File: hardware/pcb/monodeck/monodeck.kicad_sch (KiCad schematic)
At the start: 12 parts

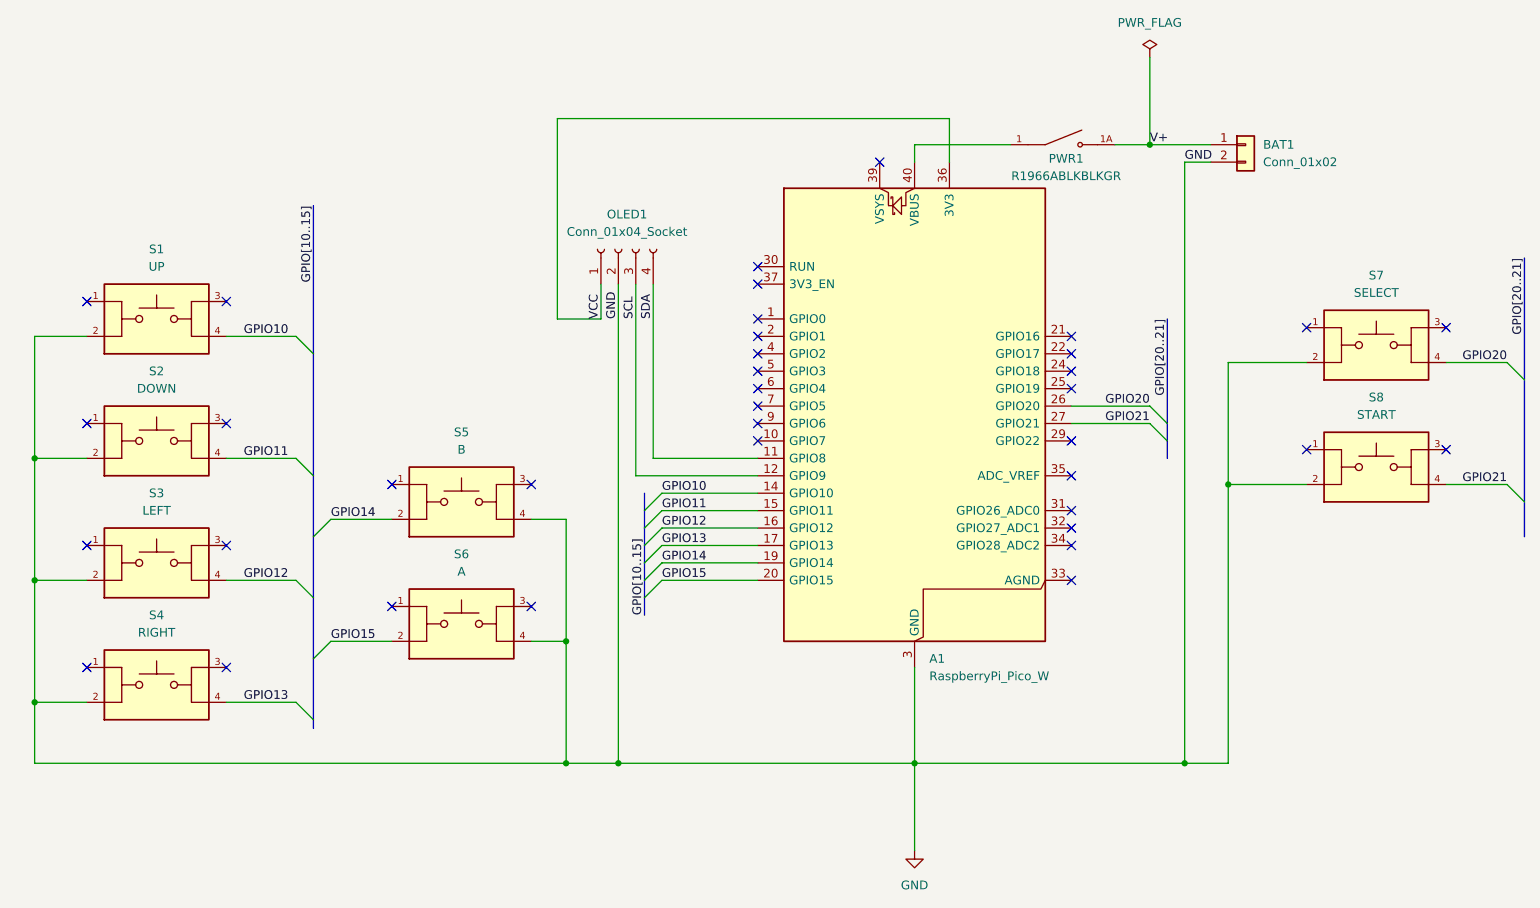
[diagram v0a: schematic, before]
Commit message: updated schematic and pcb, replaced pico smd with pin sockets
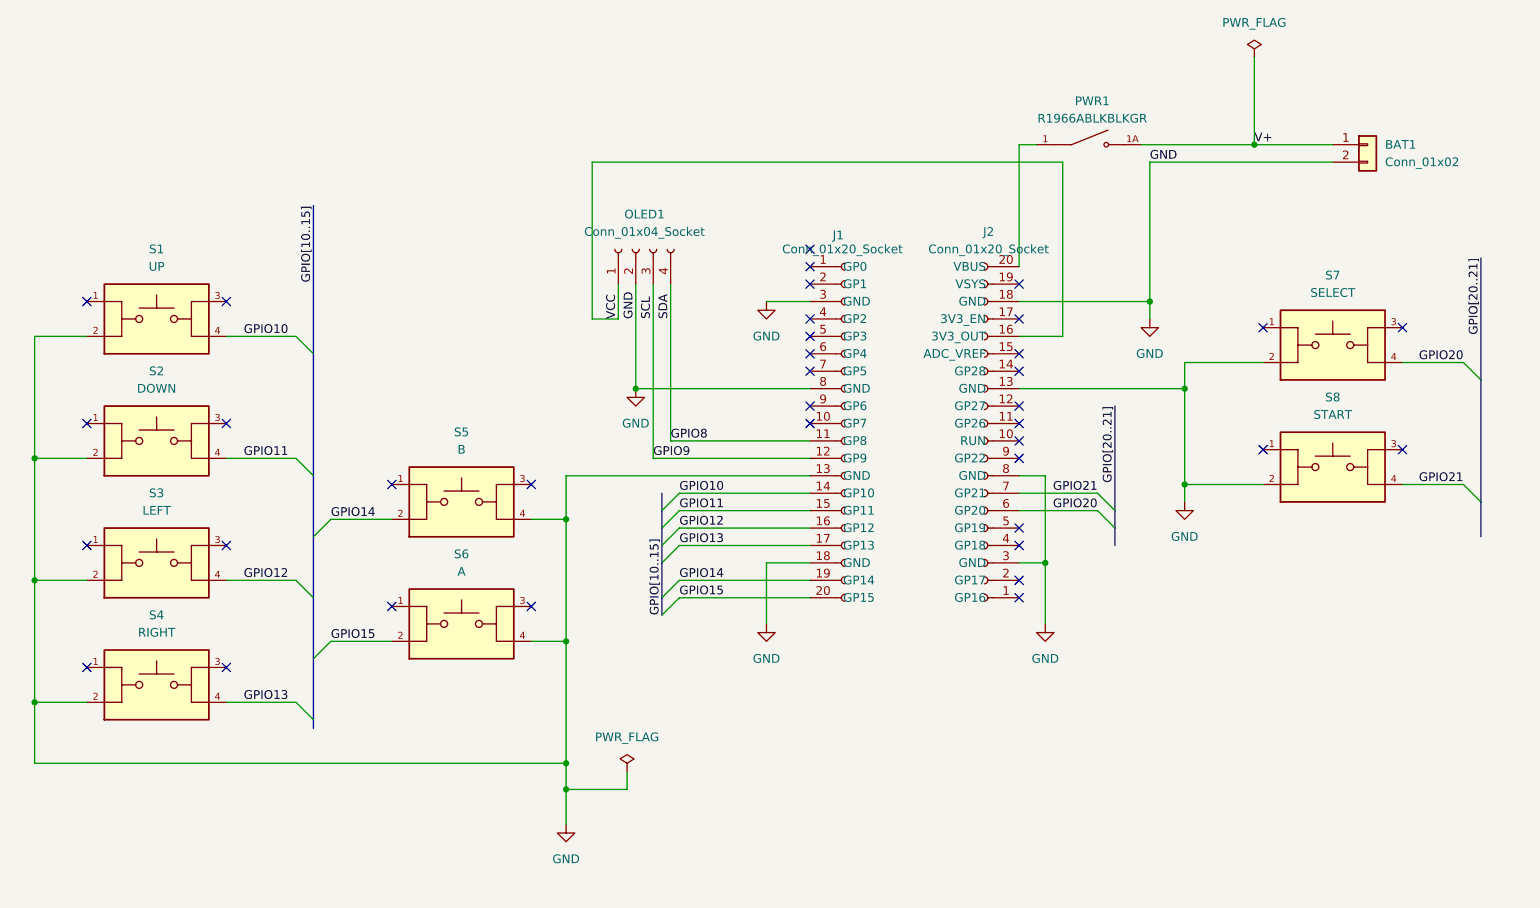
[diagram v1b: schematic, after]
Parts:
- removed A1: RaspberryPi_Pico_W, Module:RaspberryPi_Pico_W_SMD_HandSolder, symbol MCU_Module:RaspberryPi_Pico_W
- added J1, J2: Conn_01x20_Socket, Connector_PinSocket_2.54mm:PinSocket_1x20_P2.54mm_Vertical, symbol Connector:Conn_01x20_Socket
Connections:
- net GND: now also J1.13 (GND), J1.18 (GND), J1.3 (GND), J1.8 (GND), J2.13 (GND), J2.18 (GND), J2.3 (GND), J2.8 (GND)
- net GPIO10: now also J1.14 (GP10)
- net GPIO11: now also J1.15 (GP11)
- net GPIO12: now also J1.16 (GP12)
- net GPIO13: now also J1.17 (GP13)
- net GPIO14: now also J1.19 (GP14)
- net GPIO15: now also J1.20 (GP15)
- net GPIO20: now also J2.6 (GP20)
- net GPIO21: now also J2.7 (GP21)
- net VCC: now also J2.16 (3V3_OUT)
- net at PWR1.1: now also J2.20 (VBUS)
- net SCL renamed GPIO9
- net GPIO9: now also J1.12 (GP9)
- net SDA renamed GPIO8
- net GPIO8: now also J1.11 (GP8)
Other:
- moved on the sheet: BAT1, OLED1, PWR1, S7, S8

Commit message: added tp4056 module to the circuit
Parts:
- added U1: TP4056, TP4056-Module:TP4056-Module, symbol TP4056-Module:Tp4056-Module
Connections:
- net GND: now also U1.4 (Vout-), U1.6 (B-)
- net V+: now also J2.20 (VBUS); no longer BAT1.1 (Pin_1)
- net at PWR1.1: now also U1.3 (Vout+); no longer J2.20 (VBUS)
- new net: BAT1.1 (Pin_1), U1.5 (B+)
- no-connect marks 37 -> 38
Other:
- moved on the sheet: BAT1, PWR1

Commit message: finished first iteration of pcb
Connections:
- net GND: no longer J1.13 (GND), J1.3 (GND), J1.8 (GND), J2.13 (GND), J2.18 (GND), S1.2, S2.2, S3.2, S4.2, S5.4, S6.4, S7.2, S8.2
- net GPIO11: now also S2.3; no longer S2.4
- net GPIO13: now also S4.3; no longer S4.4
- net GPIO20: now also S5.1; no longer S7.4
- net GPIO21: now also S6.1; no longer S8.4
- net GND1: now reaches S1.1
- net GND1: now also J1.3 (GND), S2.1, S2.2, S3.1, S4.2
- net GPIO2: now reaches J1.4 (GP2)
- net GPIO2: now also S8.3
- net GPIO3: now reaches J1.5 (GP3)
- net GPIO3: now also S7.3
- net GPIO14: no longer names the net of J1.19 (GP14)
- net GPIO14: no longer S5.2
- net GPIO15: no longer names the net of J1.20 (GP15)
- net GPIO15: no longer S6.2
- new net GND2: J2.18 (GND), S5.4, S6.4, S7.2, S8.2
- no-connect marks 38 -> 40
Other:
- moved on the sheet: S5, S6

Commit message: update: edited gnd plane to connect all gnd nets
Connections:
- net GND1 is gone; now on net GND: J1.3 (GND), S1.1, S2.1, S2.2, S3.1, S4.2
- net GND2 is gone; now on net GND: J2.18 (GND), S5.4, S6.4, S7.2, S8.2

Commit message: updated pcb and dpad pin mapping for efficient routing
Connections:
- net GPIO10: now also S4.3; no longer S1.4
- net GPIO11: now also S1.4; no longer S2.3
- net GPIO12: now also S2.3; no longer S3.4
- net GPIO13: now also S3.4; no longer S4.3
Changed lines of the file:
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@@
 		)
 	)
-	(label "GPIO11"
+	(label "GPIO12"
 		(at 58.42 96.52 180)
 		(effects
@@
 		)
 	)
-	(label "GPIO10"
+	(label "GPIO11"
 		(at 50.8 83.82 0)
 		(effects
@@
 		)
 	)
-	(label "GPIO13"
+	(label "GPIO10"
 		(at 50.8 132.08 0)
 		(effects
@@
 		)
 	)
-	(label "GPIO12"
+	(label "GPIO13"
 		(at 50.8 119.38 0)
 		(effects
